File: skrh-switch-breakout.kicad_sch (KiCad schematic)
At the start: 0 parts

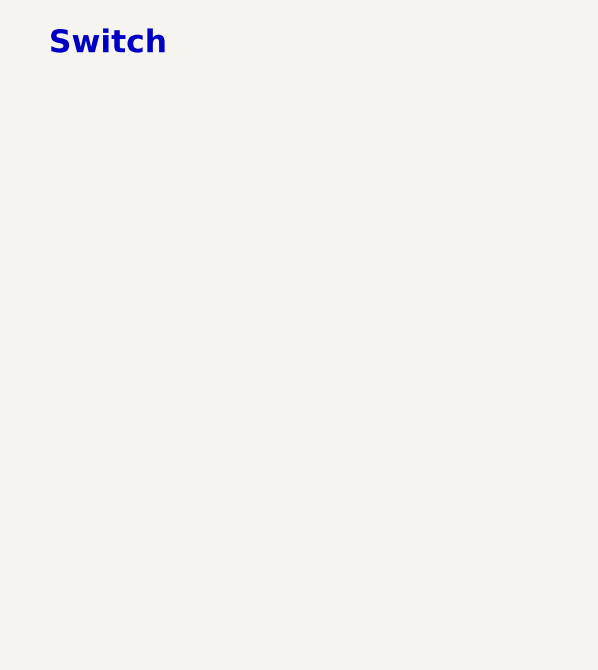
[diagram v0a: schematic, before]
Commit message: add breakout for left side
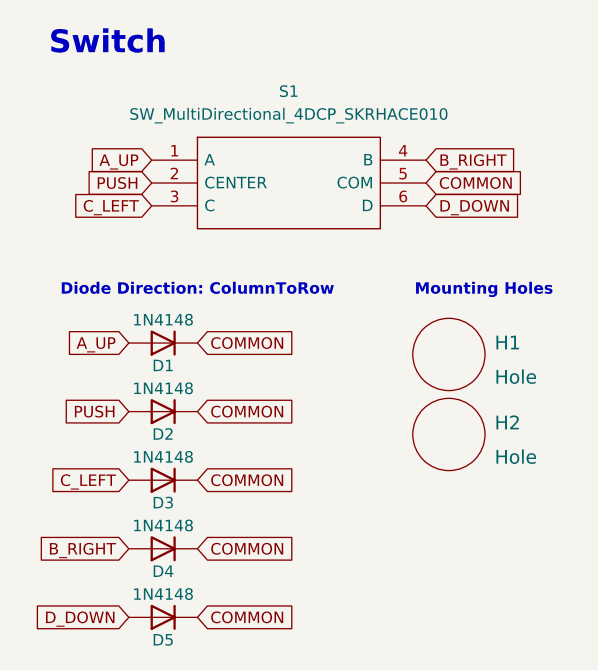
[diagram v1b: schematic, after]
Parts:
- added D1, D2, D3, D4, D5: 1N4148, Keebrary:Diode_D_SOD-123_Silkless_Reversible, symbol Diode:1N4148
- added H1, H2: Hole, Keebrary:MountingHole_2.3mm_M2_Threaded_ISO14580_Pad, symbol Keebrary:Hole
- added S1: SW_MultiDirectional_4DCP_SKRHACE010, Keebrary:SW_MultiDirectional_4DCP_SKRHACE010_SMD_7.5x7.5mm_Breakout, symbol Keebrary:SW_MultiDirectional_4DCP_SKRHACE010
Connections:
- new net A_UP: D1.2 (A), S1.1 (A)
- new net B_RIGHT: D4.2 (A), S1.4 (B)
- new net COMMON: D1.1 (K), D2.1 (K), D3.1 (K), D4.1 (K), D5.1 (K), S1.5 (COM)
- new net C_LEFT: D3.2 (A), S1.3 (C)
- new net D_DOWN: D5.2 (A), S1.6 (D)
- new net PUSH: D2.2 (A), S1.2 (CENTER)
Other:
- note added: "Diode Direction: ColumnToRow"
- note added: "Mounting Holes"
